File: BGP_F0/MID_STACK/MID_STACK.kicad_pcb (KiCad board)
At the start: 2 copper layers, 20 x 26 mm, 7 parts, among them P1 CONN_01X04, P2 CONN_01X09

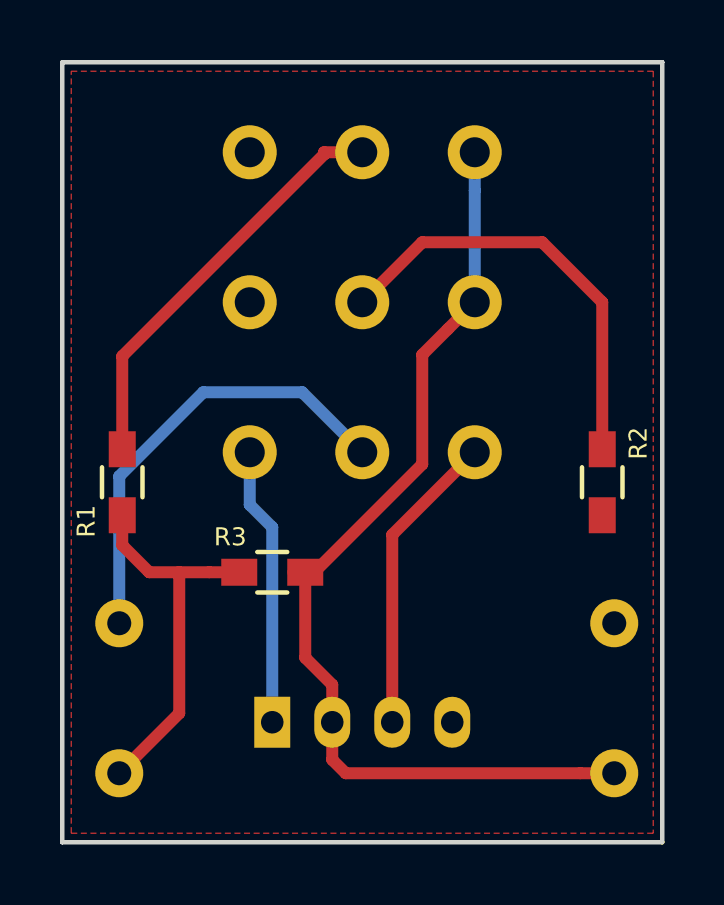
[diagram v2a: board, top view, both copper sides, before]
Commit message: F0 - Fixed Mid Stack, BT, BUF
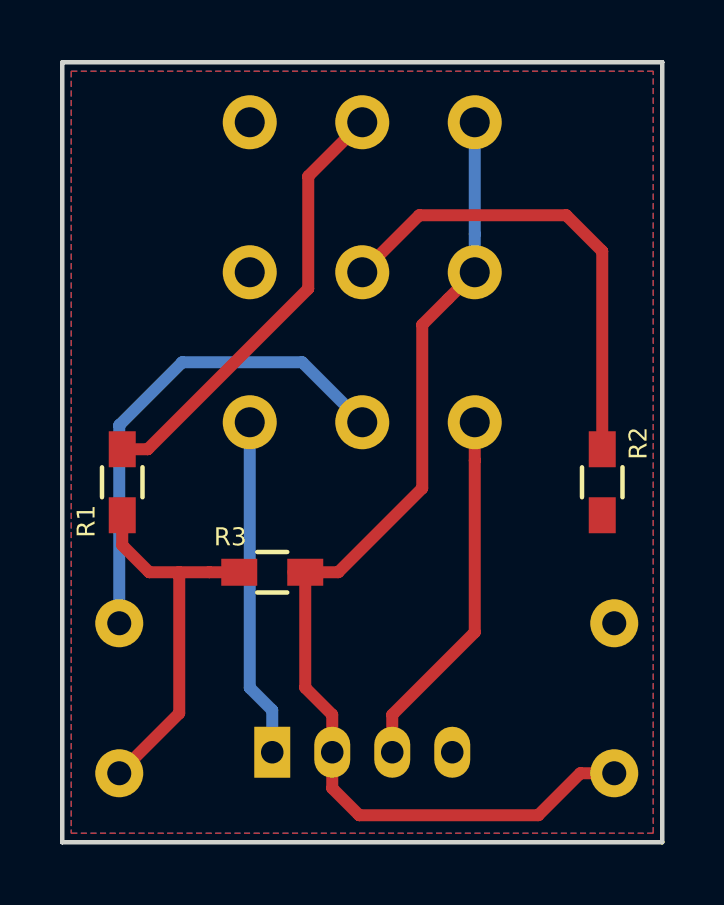
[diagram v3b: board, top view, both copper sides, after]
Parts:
- moved P1 1.00 mm to (172.0, 115.0)
- moved P2 1.00 mm to (171.2, 94.0)
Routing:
- net /F1_1: track 33.1 -> 36.3 mm
- net /MID_I: track 9.31 -> 11.4 mm
- net /MID_O: track 10.1 -> 12.1 mm
- net /VOL2: track 15.0 -> 16.4 mm
- net /F2_2: track 14.6 -> 15.9 mm
- net /F1_2: track 14.0 -> 14.7 mm
- added copper zone on B.Cu, net (none)
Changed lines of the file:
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@@
   (general
     (links 13)
-    (no_connects 5)
-    (area 164.924999 91.924999 185.075001 118.075001)
+    (no_connects 0)
+    (area 164.924999 88.649999 185.325001 118.155)
     (thickness 1.6)
     (drawings 8)
-    (tracks 39)
+    (tracks 43)
     (zones 0)
     (modules 7)
@@
   )
   (module LIBS:Potentiometer_Alpha_Tripple_Vertical_Dual_Shaft (layer B.Cu)
-    (at 171.25 95 90)
+    (at 171.25 94 90)
     (descr "Potentiometer, vertically mounted, Omeg PC16PU, Omeg PC16PU, Omeg PC16PU, Vishay/Spectrol 248GJ/249GJ Single, Vishay/Spectrol 248GJ/249GJ Single, Vishay/Spectrol 248GJ/249GJ Single, Vishay/Spectrol 248GH/249GH Single, Vishay/Spectrol 148/149 Single, Vishay/Spectrol 148/149 Single, Vishay/Spectrol 148/149 Single, Vishay/Spectrol 148A/149A Single with mounting plates, Vishay/Spectrol 148/149 Double, Vishay/Spectrol 148A/149A Double with mounting plates, Piher PC-16 Single, Piher PC-16 Single, Piher PC-16 Single, Piher PC-16SV Single, Piher PC-16 Double, Piher PC-16 Triple, Piher T16H Single, Piher T16L Single, Piher T16H Double, Alps RK163 Single, Alps RK163 Double, Alps RK097 Single, Alps RK097 Double, http://www.alps.com/prod/info/E/HTML/Potentiometer/RotaryPotentiometers/RK097/RK09712100AV.html")
     (tags "Potentiometer vertical  Omeg PC16PU  Omeg PC16PU  Omeg PC16PU  Vishay/Spectrol 248GJ/249GJ Single  Vishay/Spectrol 248GJ/249GJ Single  Vishay/Spectrol 248GJ/249GJ Single  Vishay/Spectrol 248GH/249GH Single  Vishay/Spectrol 148/149 Single  Vishay/Spectrol 148/149 Single  Vishay/Spectrol 148/149 Single  Vishay/Spectrol 148A/149A Single with mounting plates  Vishay/Spectrol 148/149 Double  Vishay/Spectrol 148A/149A Double with mounting plates  Piher PC-16 Single  Piher PC-16 Single  Piher PC-16 Single  Piher PC-16SV Single  Piher PC-16 Double  Piher PC-16 Triple  Piher T16H Single  Piher T16L Single  Piher T16H Double  Alps RK163 Single  Alps RK163 Double  Alps RK097 Single  Alps RK097 Double Dual Shaft")
-    (fp_text reference P2 (at -5.2 11.35 90) (layer B.SilkS)
+    (fp_text reference P2 (at -15.4 9.95 180) (layer B.SilkS)
       (effects (font (size 0.6 0.6) (thickness 0.15)) (justify mirror))
     )
@@
   )
   (module Connectors_JST:JST_PH_B4B-PH-K_04x2.00mm_Straight (layer B.Cu)
-    (at 172 114)
+    (at 172 115)
     (descr "JST PH series connector, B4B-PH-K, top entry type, through hole, Datasheet: http://www.jst-mfg.com/product/pdf/eng/ePH.pdf")
     (tags "connector jst ph")
@@
   (gr_line (start 165 92) (end 165 118) (layer Edge.Cuts) (width 0.15))
   (gr_line (start 185 92) (end 165 92) (layer Edge.Cuts) (width 0.15))
-  (segment (start 169.7 103) (end 173 103) (width 0.4) (layer B.Cu) (net 1))
-  (segment (start 173 103) (end 175 105) (width 0.4) (layer B.Cu) (net 1))
-  (segment (start 166.9 105.8) (end 169.7 103) (width 0.4) (layer B.Cu) (net 1))
-  (segment (start 166.9 110.7) (end 166.9 105.8) (width 0.4) (layer B.Cu) (net 1))
+  (segment (start 169 102) (end 173 102) (width 0.4) (layer B.Cu) (net 1))
+  (segment (start 173 102) (end 175 104) (width 0.4) (layer B.Cu) (net 1))
+  (segment (start 166.9 104.1) (end 169 102) (width 0.4) (layer B.Cu) (net 1))
+  (segment (start 166.9 110.7) (end 166.9 104.1) (width 0.4) (layer B.Cu) (net 1))
   (segment (start 167.9 109) (end 168.9 109) (width 0.4) (layer F.Cu) (net 2))
   (segment (start 168.9 109) (end 169.9 109) (width 0.4) (layer F.Cu) (net 2))
@@
   (segment (start 169.9 109) (end 170.9 109) (width 0.4) (layer F.Cu) (net 2))
   (segment (start 167 108.1) (end 167.9 109) (width 0.4) (layer F.Cu) (net 2))
-  (segment (start 173.1 109) (end 173.4 109) (width 0.4) (layer F.Cu) (net 3))
-  (segment (start 173.4 109) (end 177 105.4) (width 0.4) (layer F.Cu) (net 3))
-  (segment (start 177 105.4) (end 177 101.75) (width 0.4) (layer F.Cu) (net 3))
-  (segment (start 177 101.75) (end 177.850001 100.899999) (width 0.4) (layer F.Cu) (net 3))
-  (segment (start 177.850001 100.899999) (end 178.75 100) (width 0.4) (layer F.Cu) (net 3))
-  (segment (start 174 114) (end 174 115.25) (width 0.4) (layer F.Cu) (net 3))
-  (segment (start 174 115.25) (end 174.45 115.7) (width 0.4) (layer F.Cu) (net 3))
-  (segment (start 174.45 115.7) (end 182.26863 115.7) (width 0.4) (layer F.Cu) (net 3))
-  (segment (start 182.26863 115.7) (end 183.4 115.7) (width 0.4) (layer F.Cu) (net 3))
-  (segment (start 174 114) (end 174 112.75) (width 0.4) (layer F.Cu) (net 3))
-  (segment (start 174 112.75) (end 173.1 111.85) (width 0.4) (layer F.Cu) (net 3))
-  (segment (start 173.1 111.85) (end 173.1 109) (width 0.4) (layer F.Cu) (net 3))
-  (segment (start 178.75 95) (end 178.75 96.272792) (width 0.4) (layer B.Cu) (net 3))
-  (segment (start 178.75 96.272792) (end 178.75 100) (width 0.4) (layer B.Cu) (net 3))
+  (segment (start 183.4 115.7) (end 182.26863 115.7) (width 0.4) (layer F.Cu) (net 3))
+  (segment (start 182.26863 115.7) (end 180.86863 117.1) (width 0.4) (layer F.Cu) (net 3))
+  (segment (start 180.86863 117.1) (end 174.9 117.1) (width 0.4) (layer F.Cu) (net 3))
+  (segment (start 174.9 117.1) (end 174 116.2) (width 0.4) (layer F.Cu) (net 3))
+  (segment (start 174 116.2) (end 174 115) (width 0.4) (layer F.Cu) (net 3))
+  (segment (start 174 115) (end 174 113.75) (width 0.4) (layer F.Cu) (net 3))
+  (segment (start 174 113.75) (end 173.1 112.85) (width 0.4) (layer F.Cu) (net 3))
+  (segment (start 173.1 112.85) (end 173.1 109) (width 0.4) (layer F.Cu) (net 3))
+  (segment (start 173.1 109) (end 174.2 109) (width 0.4) (layer F.Cu) (net 3))
+  (segment (start 174.2 109) (end 177 106.2) (width 0.4) (layer F.Cu) (net 3))
+  (segment (start 177 100.75) (end 177.850001 99.899999) (width 0.4) (layer F.Cu) (net 3))
+  (segment (start 177 106.2) (end 177 100.75) (width 0.4) (layer F.Cu) (net 3))
+  (segment (start 177.850001 99.899999) (end 178.75 99) (width 0.4) (layer F.Cu) (net 3))
+  (segment (start 178.75 99) (end 178.75 97.727208) (width 0.4) (layer B.Cu) (net 3))
+  (segment (start 178.75 97.727208) (end 178.75 94) (width 0.4) (layer B.Cu) (net 3))
   (segment (start 173.1 109) (end 172.7 109) (width 0.4) (layer F.Cu) (net 3))
-  (segment (start 172 114) (end 172 107.5) (width 0.4) (layer B.Cu) (net 5))
-  (segment (start 172 107.5) (end 171.25 106.75) (width 0.4) (layer B.Cu) (net 5))
-  (segment (start 171.25 106.75) (end 171.25 105) (width 0.4) (layer B.Cu) (net 5))
-  (segment (start 176 114) (end 176 107.75) (width 0.4) (layer F.Cu) (net 6))
-  (segment (start 176 107.75) (end 178.75 105) (width 0.4) (layer F.Cu) (net 6))
-  (segment (start 167 104.9) (end 167 101.8) (width 0.4) (layer F.Cu) (net 7))
-  (segment (start 167 101.8) (end 173.727208 95.072792) (width 0.4) (layer F.Cu) (net 7))
-  (segment (start 173.727208 95.072792) (end 173.727208 95) (width 0.4) (layer F.Cu) (net 7))
-  (segment (start 173.727208 95) (end 175 95) (width 0.4) (layer F.Cu) (net 7))
-  (segment (start 183 104.9) (end 183 100) (width 0.4) (layer F.Cu) (net 8))
-  (segment (start 183 100) (end 181 98) (width 0.4) (layer F.Cu) (net 8))
-  (segment (start 181 98) (end 177 98) (width 0.4) (layer F.Cu) (net 8))
-  (segment (start 177 98) (end 175 100) (width 0.4) (layer F.Cu) (net 8))
+  (segment (start 172 115) (end 172 113.6) (width 0.4) (layer B.Cu) (net 5))
+  (segment (start 172 113.6) (end 171.25 112.85) (width 0.4) (layer B.Cu) (net 5))
+  (segment (start 171.25 112.85) (end 171.25 104) (width 0.4) (layer B.Cu) (net 5))
+  (segment (start 171.2 104.05) (end 171.25 104) (width 0.4) (layer F.Cu) (net 5))
+  (segment (start 176 115) (end 176 113.75) (width 0.4) (layer F.Cu) (net 6))
+  (segment (start 176 113.75) (end 178.75 111) (width 0.4) (layer F.Cu) (net 6))
+  (segment (start 178.75 111) (end 178.75 105.272792) (width 0.4) (layer F.Cu) (net 6))
+  (segment (start 178.75 105.272792) (end 178.75 104) (width 0.4) (layer F.Cu) (net 6))
+  (segment (start 175 94) (end 173.2 95.8) (width 0.4) (layer F.Cu) (net 7))
+  (segment (start 173.2 95.8) (end 173.2 99.55) (width 0.4) (layer F.Cu) (net 7))
+  (segment (start 173.2 99.55) (end 167.85 104.9) (width 0.4) (layer F.Cu) (net 7))
+  (segment (start 167.85 104.9) (end 167 104.9) (width 0.4) (layer F.Cu) (net 7))
+  (segment (start 181.8 97.1) (end 183 98.3) (width 0.4) (layer F.Cu) (net 8))
+  (segment (start 183 98.3) (end 183 104.9) (width 0.4) (layer F.Cu) (net 8))
+  (segment (start 176.9 97.1) (end 181.8 97.1) (width 0.4) (layer F.Cu) (net 8))
+  (segment (start 175 99) (end 176.9 97.1) (width 0.4) (layer F.Cu) (net 8))
   (zone (net 4) (net_name /Vref) (layer F.Cu) (hatch edge 0.508)
     (connect_pads (clearance 0.3))
@@
     (polygon
       (pts
-        (xy 184.7 117.7) (xy 165.3 117.7) (xy 165.3 92.3) (xy 184.7 92.3)
+        (xy 184.7 92.3) (xy 165.3 92.3) (xy 165.3 117.7) (xy 184.7 117.7)
       )
     )
+  )
+  (zone (net 0) (net_name "") (layer B.Cu) (hatch edge 0.508)
+    (connect_pads (clearance 0.3))
+    (min_thickness 0.3)
+    (fill yes (arc_segments 16) (thermal_gap 0.3) (thermal_bridge_width 0.6))
+    (polygon
+      (pts
+        (xy 184.7 92.3) (xy 165.3 92.3) (xy 165.3 117.7) (xy 184.7 117.7)
+      )
+    )

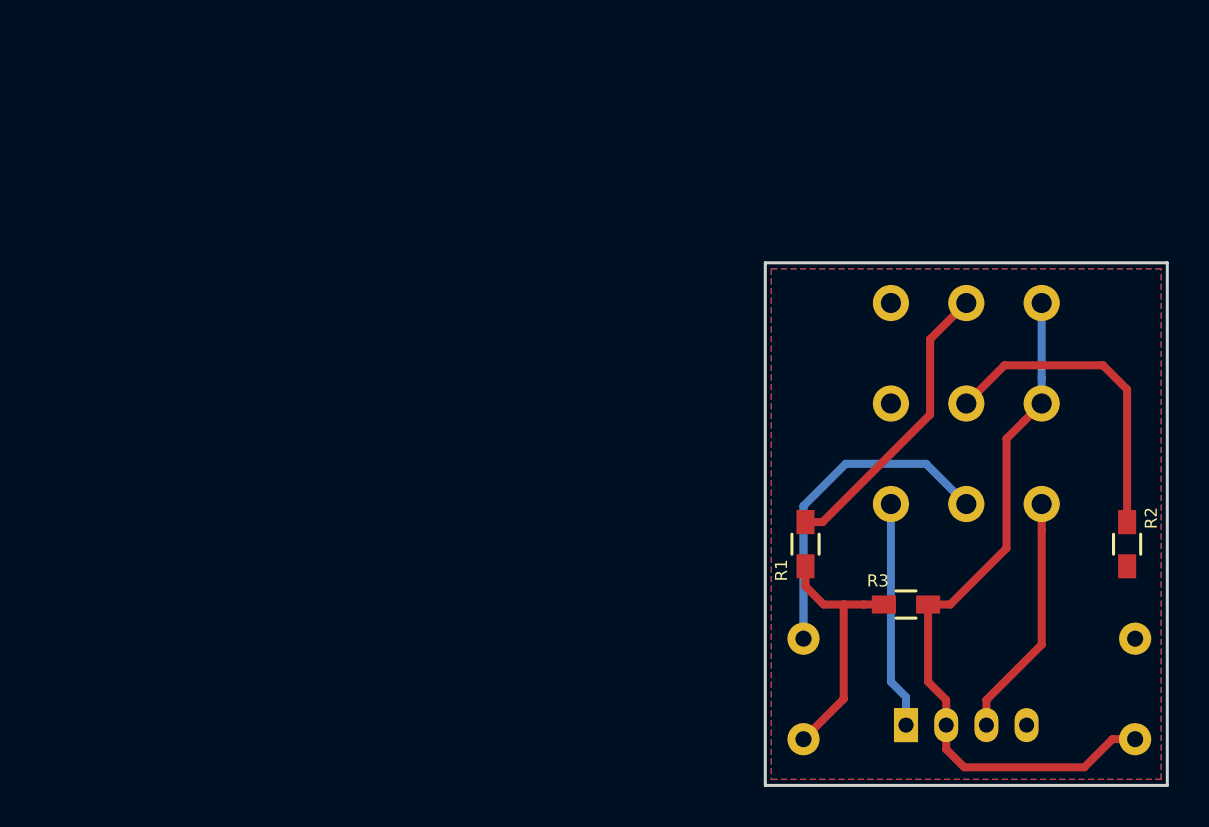
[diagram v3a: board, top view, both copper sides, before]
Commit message: MM Gerbers Finished, Mid Stack Ammended J0
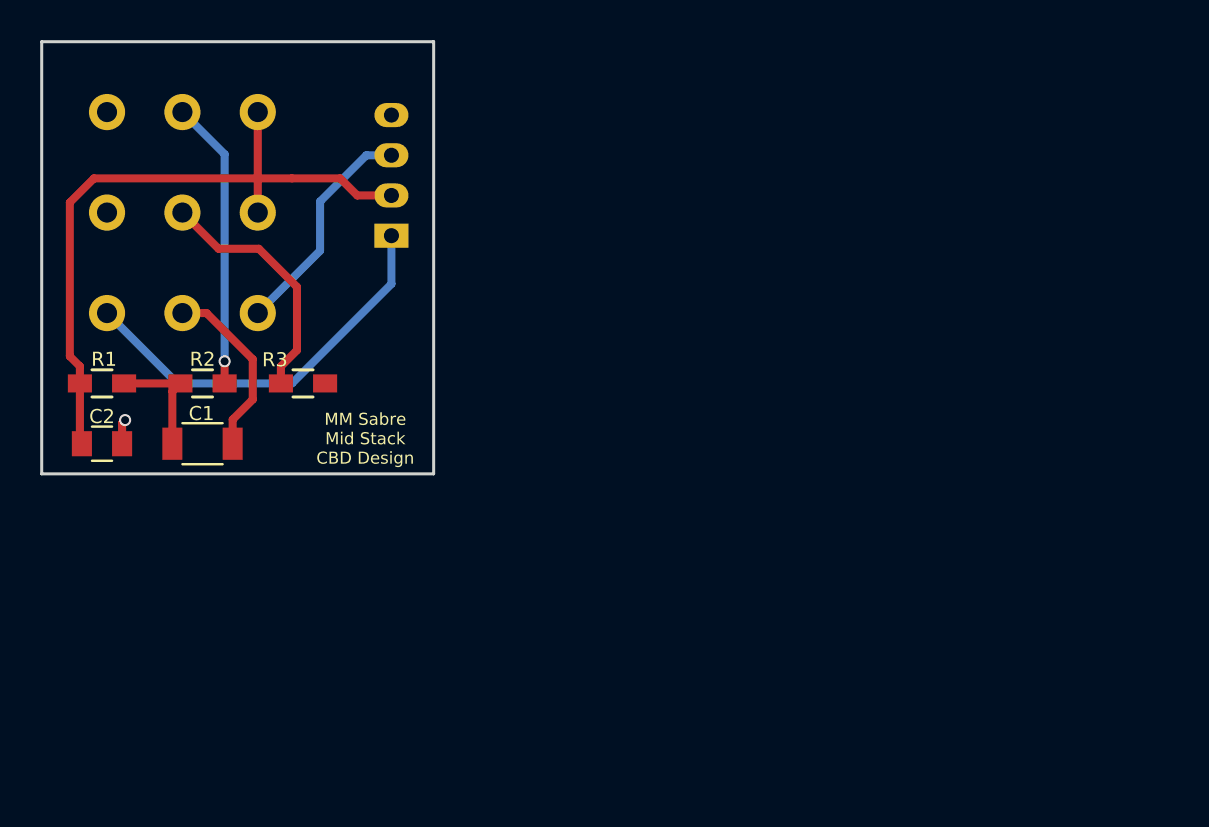
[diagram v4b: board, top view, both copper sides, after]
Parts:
- removed P2: CONN_01X09, LIBS:Potentiometer_Alpha_Tripple_Vertical_Dual_Shaft
- added J1: Conn_01x04_Male, Connectors_JST:JST_PH_B4B-PH-K_04x2.00mm_Straight, B.Cu at (146.4, 90.7)
- C1: footprint Capacitor_THT:C_Rect_L7.2mm_W2.5mm_P5.00mm_FKS2_FKP2_MKS2_MKP2 -> Capacitors_SMD:C_1206; moved to F.Cu
- C2: footprint Capacitor_THT:C_Rect_L7.2mm_W2.5mm_P5.00mm_FKS2_FKP2_MKS2_MKP2 -> Capacitors_SMD:C_0805; moved to F.Cu
- P1: value CONN_01X04 -> CONN_01X09; footprint Connectors_JST:JST_PH_B4B-PH-K_04x2.00mm_Straight -> LIBS:Potentiometer_Alpha_Tripple_Vertical_Dual_Shaft
- R1: value 4.7k -> 200k
- R2: value 4.7k -> 10k
- R3: value 100k -> 10k
- moved C2 53.5 mm to (132.0, 101.0), turned to 0 degrees
- moved P1 50.1 mm to (132.2, 84.5), turned to 90 degrees
- moved R2 46.7 mm to (137.0, 98.0), turned to 0 degrees
- moved R1 35.9 mm to (132.0, 98.0), turned to 180 degrees
- moved R3 32.0 mm to (142.0, 98.0)
- moved C1 31.4 mm to (137.0, 101.0), turned to 180 degrees
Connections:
- C2 pad 1: /F1_1 -> /MID_R
- P1 pad 1: /MID_I -> Net-(P1-Pad1)
- P1 pad 2: /F1_1 -> /F1_2
- P1 pad 3: /MID_O -> /MID_R
- P1 pad 4: /Vref -> Net-(P1-Pad4)
- R1 pad 2: /F1_2 -> /MID_R
- R2 pad 1: /F2_2 -> Net-(C1-Pad2)
- R2 pad 2: /Vref -> /F1_2
- R3 pad 1: Net-(C1-Pad2) -> /F2_2
- R3 pad 2: /F1_1 -> /Vref
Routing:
- net /F1_1: track 36.3 -> 0.00 mm
- net /MID_R: track 0.00 -> 34.2 mm
- net /MID_I: track 11.4 -> 20.1 mm
- net /VOL2: track 16.4 -> 9.07 mm
- net Net-(C1-Pad2): track 12.8 -> 6.25 mm
- net /F2_2: track 15.9 -> 12.4 mm
- net /Vref: track 0.00 -> 1.24 mm, vias 0 -> 1
- net /MID_O: track 12.1 -> 11.3 mm
- net /F1_2: track 14.7 -> 14.4 mm, vias 0 -> 1
- added copper zone on B.Cu, net /Vref
- removed copper zone on B.Cu, net (none)
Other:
- board size 20 x 26 mm -> 19.5 x 21.5 mm
- board text added: "MM Sabre Mid Stack CBD Design"

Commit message: Minor tweaks for MM/F0 - gerbers ready to go out
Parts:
- J1: footprint Connectors_JST:JST_PH_B4B-PH-K_04x2.00mm_Straight -> Pin_Headers:Pin_Header_Straight_1x04
- moved J1 7.30 mm to (144.5, 83.6), turned to 180 degrees
- moved C2 0.60 mm to (132.0, 100.4)
- moved C1 0.50 mm to (137.0, 100.5)
- moved R1 0.50 mm to (132.0, 97.5)
- moved R2 0.50 mm to (137.0, 97.5)
- moved R3 0.50 mm to (142.0, 97.5)
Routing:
- net /MID_I: track 20.1 -> 27.3 mm
- net /MID_O: track 11.3 -> 7.81 mm
- net /MID_R: track 34.2 -> 32.0 mm
- net /Vref: track 1.24 -> 0.00 mm, vias 1 -> 0
- net /F2_2: track 12.4 -> 11.9 mm
- net /F1_2: track 14.4 -> 13.9 mm
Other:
- board size 19.5 x 21.5 mm -> 17.5 x 21.5 mm
- board text removed: "MM Sabre Mid Stack CBD Design"
